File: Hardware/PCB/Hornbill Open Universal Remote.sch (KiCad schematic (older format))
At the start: 66 parts, among them CON1 USB-MINI-B, M1 ESP-WROOM-32, P1 CONN_01X14, P10 CONN_01X14, P11 CONN_01X14, P12 CONN_01X14, P13 CONN_01X14, P14 CONN_01X14, P15 CONN_01X14, P2 CONN_01X03, P3 CONN_01X14, P4 CONN_01X14, P5 CONN_01X14, P6 CONN_01X14, P7 CONN_01X14, P8 CONN_01X14, P9 CONN_01X14, Q1 IRLML5203, Q2 Q_NPN_BEC, Q3 S8050, Q4 S8050, SW1 SW_PUSH, SW2 SW_PUSH, U1 AP2112K, U2 OSH_Symbol, U3 EE_Logo, U4 EE_Logo, U5 MountingHole, U6 MountingHole, U7 MountingHole, U8 MountingHole, U9 CP2104, Y1 32.768KHz RTC Crystal

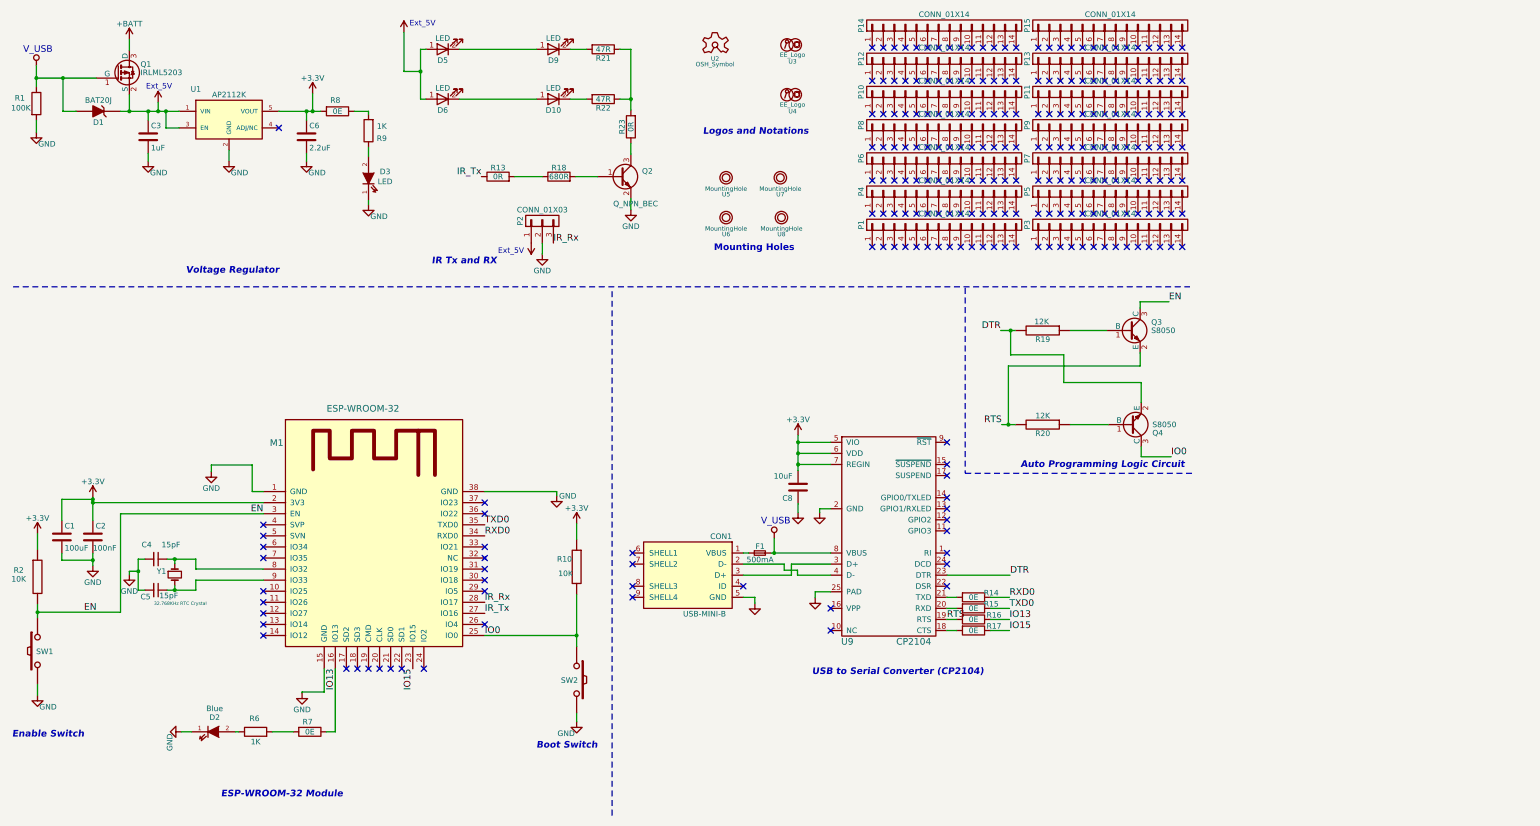
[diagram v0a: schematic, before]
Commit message: Hornbill logo added for OUR
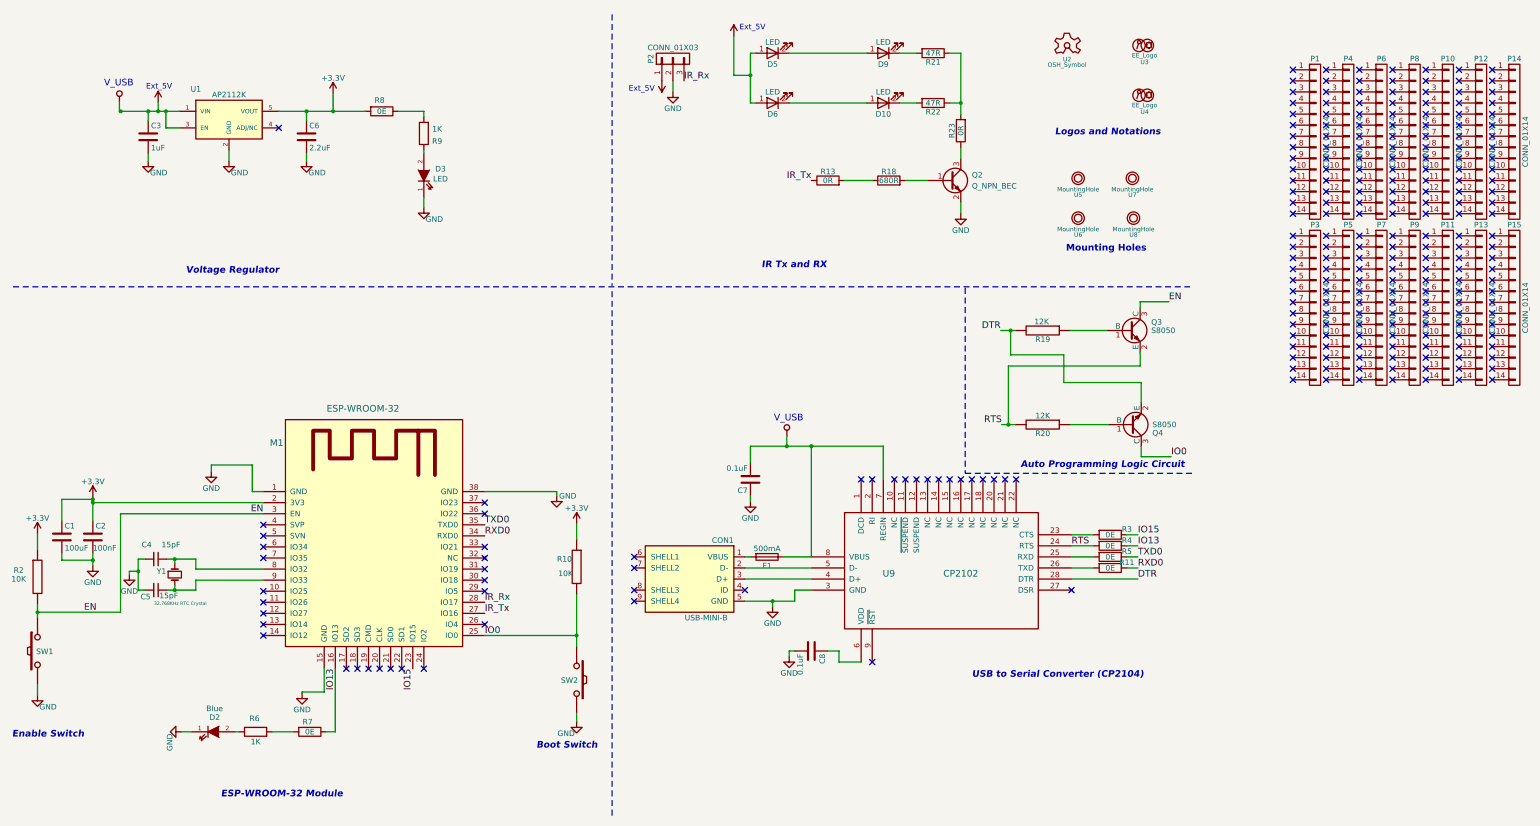
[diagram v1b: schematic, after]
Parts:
- removed D1: BAT20J, Explore:SOD-80_diode, symbol ZENER
- removed F1: 500mA, Capacitors_SMD:C_1206, symbol F_Small
- removed Q1: IRLML5203, Explore:SOT-23, symbol IRLML52303
- removed R1: 100K, Resistors_SMD:R_0603, symbol R
- removed R14, R15, R16, R17: 0E, Resistors_SMD:R_0603, symbol R
- removed U9: CP2104, Explore:CP2104, symbol CP2104-RESCUE-Hornbill_Devboard
- added C7: 0.1uF, Capacitors_SMD:C_0603, symbol C
- added F1: 500mA, Explore:Fuse_500mA, symbol Fuse
- added R11, R3, R4, R5: 0E, Resistors_SMD:R_0603, symbol R
- added U9: CP2102, Explore:cp2102_xl2, symbol CP2102
- C8: value 10uF -> 0.1uF
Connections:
- net +3V3: no longer C8.2
- net +5V: now also C7.2, F1.1, U9.7 (REGIN), U9.8 (VBUS)
- net DTR: now also U9.28 (DTR)
- net GND: now also C8.2, C7.1, U9.3 (GND); no longer C8.1
- net IO13: now also R4.1
- net IO15: now also R3.1
- net RTS: now also R4.2, U9.24 (RTS)
- net RXD0: now also R11.1
- net TXD0: now also R5.1
- net at CON1.3 (D+): now also U9.4 (D+)
- net at CON1.2 (D-): now also U9.5 (D-)
- net at CON1.1 (VBUS): now also F1.2
- new net: R3.2, U9.23 (CTS)
- new net: R5.2, U9.25 (RXD)
- new net: R11.2, U9.26 (TXD)
- new net: C8.1, U9.6 (VDD)
- no-connect marks 238 -> 242
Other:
- moved on the sheet: D10, D3, D5, D6, D9, P1, P10, P11, P12, P13, P14, P15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

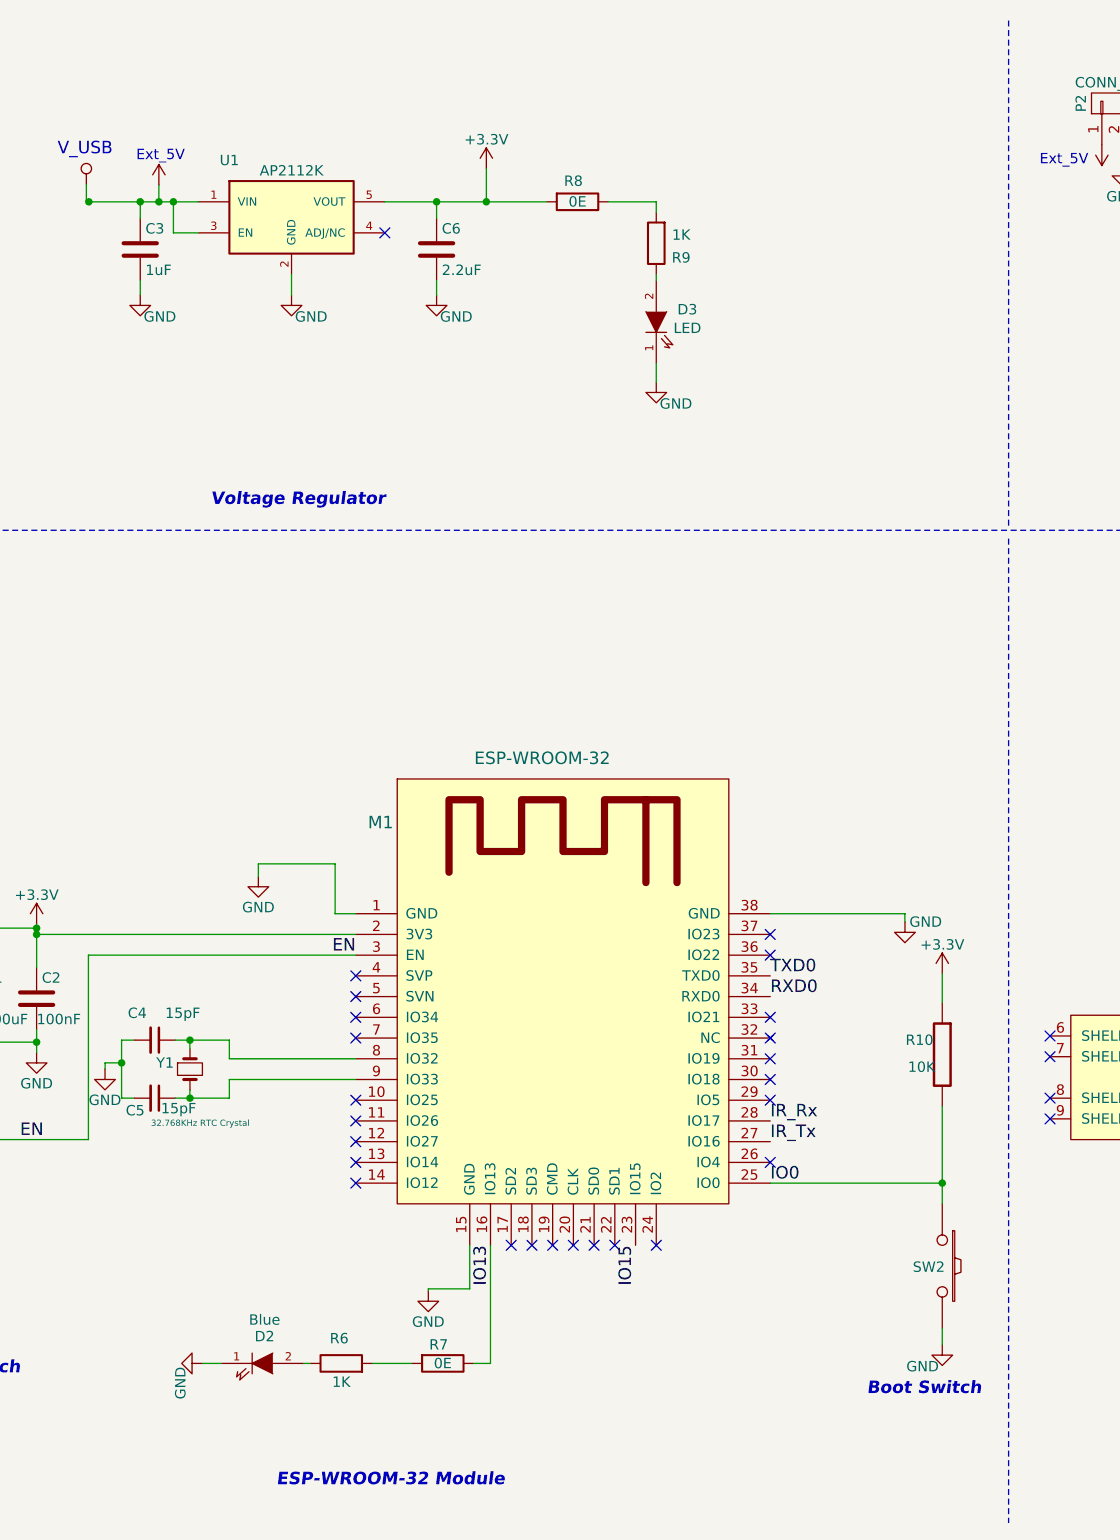
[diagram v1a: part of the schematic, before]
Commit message: IO pins taken out
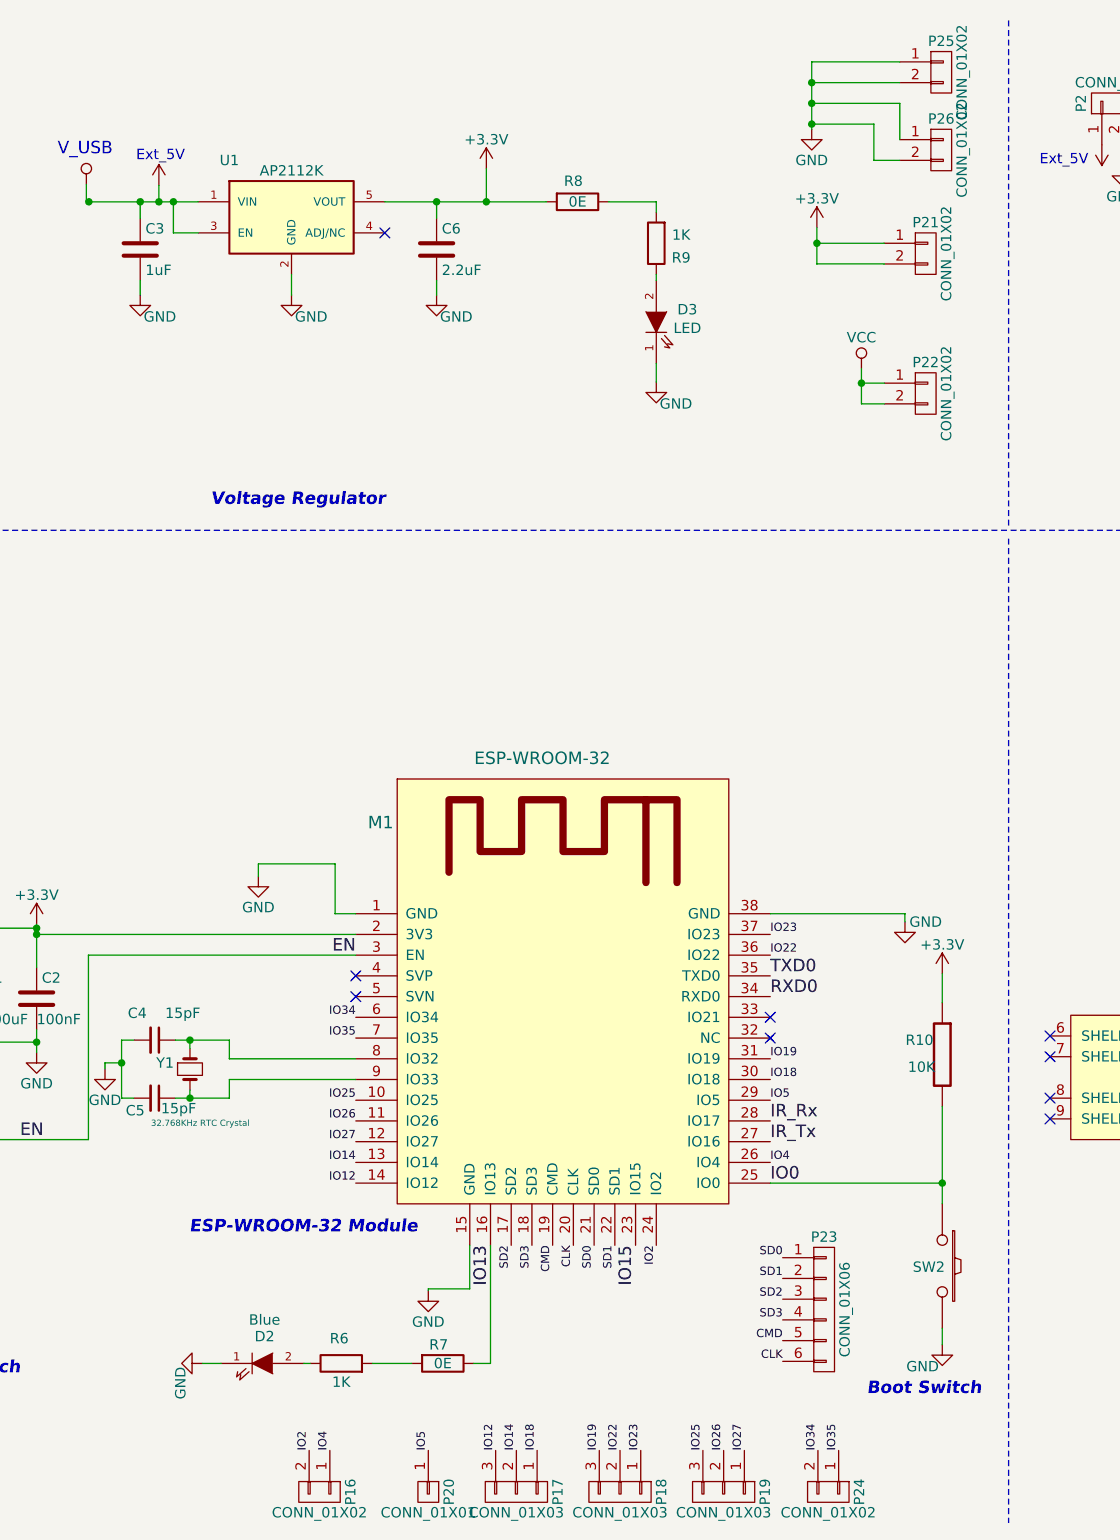
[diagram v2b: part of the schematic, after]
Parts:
- added P16, P24, P25, P26: CONN_01X02, Pin_Headers:Pin_Header_Straight_1x02_Pitch2.54mm, symbol CONN_01X02
- added P17, P18, P19: CONN_01X03, Pin_Headers:Pin_Header_Straight_1x03_Pitch2.54mm, symbol CONN_01X03
- added P20: CONN_01X01, Pin_Headers:Pin_Header_Straight_1x01_Pitch2.54mm, symbol CONN_01X01
- added P21, P22: CONN_01X02, Pin_Headers:Pin_Header_Straight_2x01_Pitch2.54mm, symbol CONN_01X02
- added P23: CONN_01X06, Pin_Headers:Pin_Header_Straight_1x06_Pitch2.54mm, symbol CONN_01X06
- U3: footprint Logo:Hornbill -> Logo:Hornbill_OUR
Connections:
- net +3V3: now also P21.1 (P1), P21.2 (P2)
- net +5V: now also P22.1 (P1), P22.2 (P2)
- net GND: now also P25.1 (P1), P25.2 (P2), P26.1 (P1), P26.2 (P2)
- net IO25: now reaches M1.10 (IO25)
- net IO25: now also P19.3 (P3)
- net IO26: now reaches M1.11 (IO26)
- net IO26: now also P19.2 (P2)
- net IO27: now reaches M1.12 (IO27)
- net IO27: now also P19.1 (P1)
- net IO14: now reaches M1.13 (IO14)
- net IO14: now also P17.2 (P2)
- net IO12: now reaches M1.14 (IO12)
- net IO12: now also P17.3 (P3)
- net SD2: now reaches M1.17 (SD2)
- net SD2: now also P23.3 (P3)
- net SD3: now reaches M1.18 (SD3)
- net SD3: now also P23.4 (P4)
- net CMD: now reaches M1.19 (CMD)
- net CMD: now also P23.5 (P5)
- net CLK: now reaches M1.20 (CLK)
- net CLK: now also P23.6 (P6)
- net SD0: now reaches M1.21 (SD0)
- net SD0: now also P23.1 (P1)
- net SD1: now reaches M1.22 (SD1)
- net SD1: now also P23.2 (P2)
- net IO2: now reaches M1.24 (IO2)
- net IO2: now also P16.2 (P2)
- net IO4: now reaches M1.26 (IO4)
- net IO4: now also P16.1 (P1)
- net IO5: now reaches M1.29 (IO5)
- net IO5: now also P20.1 (P1)
- net IO18: now reaches M1.30 (IO18)
- net IO18: now also P17.1 (P1)
- net IO19: now reaches M1.31 (IO19)
- net IO19: now also P18.3 (P3)
- net IO22: now reaches M1.36 (IO22)
- net IO22: now also P18.2 (P2)
- net IO23: now reaches M1.37 (IO23)
- net IO23: now also P18.1 (P1)
- net IO34: now reaches M1.6 (IO34)
- net IO34: now also P24.2 (P2)
- net IO35: now reaches M1.7 (IO35)
- net IO35: now also P24.1 (P1)
- no-connect marks 242 -> 222
